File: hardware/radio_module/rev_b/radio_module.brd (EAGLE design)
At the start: 68.1 x 66 mm, 132 parts, among them J1 MODULE_GENERIC_DEBUGSMT, J2 TC2030-JLINK-NL, J3 U.FL-R-SMT, J4 NANO_SIM, J5 TC2030-JLINK-L, P1 MOLEX_73251-135X, P2 MOLEX_73251-135X, Q1 MOSFET-NCHANNELSMD, Q2 MOSFET-NCHANNELSMD, Q5 SI223DDS, Q6 SI223DDS, Q7 SI223DDS, Q8 MOSFET-NCHANNELSMD, U1 NUCLEUM, U10 XDOT_MODULE, U11 SAM4LC8BA, U12 UBLOX_SARA_G350, U2 TLV62130, U3 TXB0104RUT, U4 LTC2941, U5 LTC2941, U7 PCA9544AQFN-N20, U8 TLV62130, U9 LTC2941, X2 16 MHz

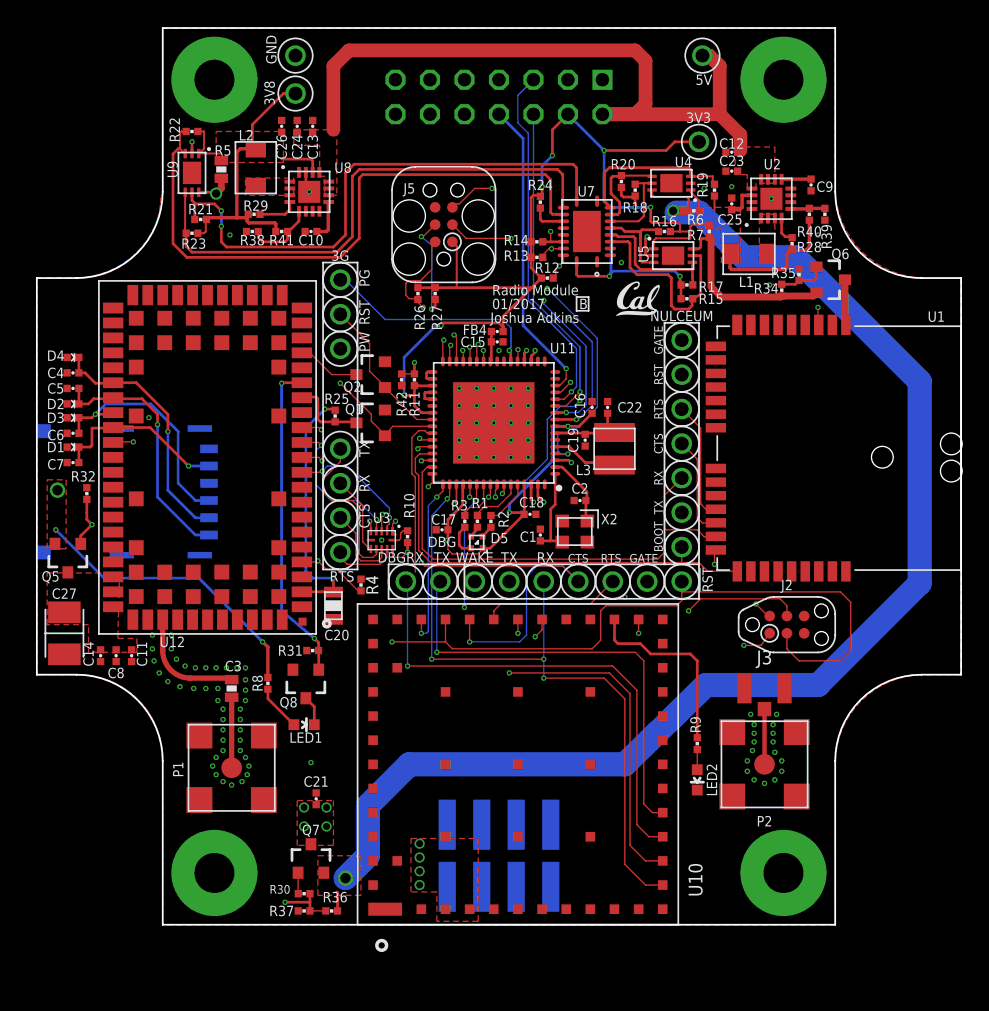
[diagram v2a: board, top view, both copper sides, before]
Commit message: added debugging signals, no more airwires
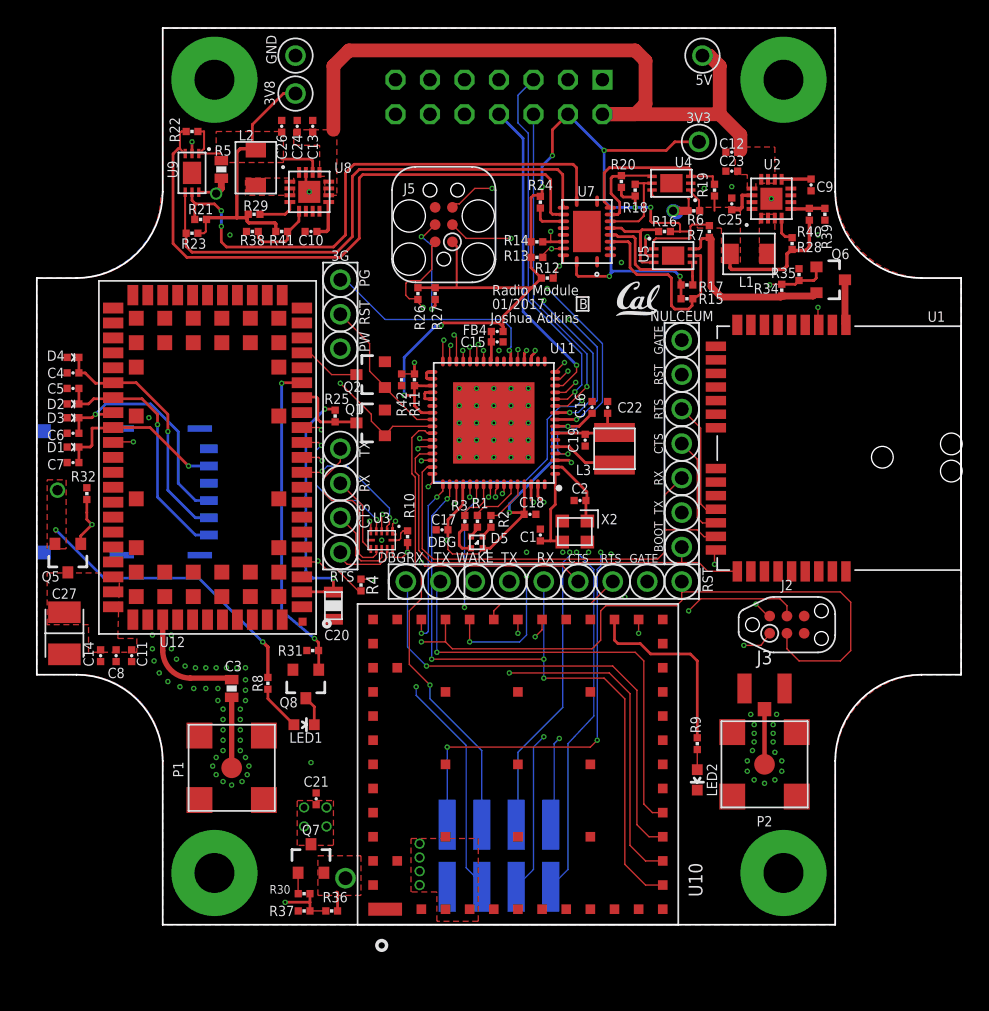
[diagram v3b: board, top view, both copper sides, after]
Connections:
- new net DBG_GPIO1: J1.16, U11.15
- new net DBG_GPIO2: J1.19, U11.16
- net !CONTROLLER_RESET: now also J1.20
- net CONTROLLER_SWDCLK: now also J1.21
- net CONTROLLER_SWDIO: now also J1.22
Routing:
- net DBG_GPIO1: track 0.00 -> 46.4 mm, vias 0 -> 4
- net DBG_GPIO2: track 0.00 -> 41.1 mm, vias 0 -> 3
- net CONTROLLER_SWDCLK: track 28.5 -> 65.1 mm, vias 4 -> 5
- net CONTROLLER_SWDIO: track 27.7 -> 61.0 mm, vias 3 -> 5
- net !CONTROLLER_RESET: track 26.6 -> 55.9 mm, vias 3 -> 4
- net DEBUG_TX: track 10.2 -> 37.3 mm, vias 1 -> 2
- net DEBUG_RX: track 11.8 -> 33.2 mm, vias 0 -> 1
- net XDOT_HOST_UART_RTS: track 23.7 -> 25.2 mm, vias 1 -> 3
- net XDOT_DBG_UART_TX: track 36.1 -> 35.3 mm
- net MOD_OUT: track 22.6 -> 23.3 mm
- net XDOT_HOST_UART_CTS: vias 3 -> 4
- net XDOT_3V3: vias 2 -> 3

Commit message: did a drc cleanup
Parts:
- moved U$1 4.06 mm to (44.1, 43.6)
- moved U3 1.09 mm to (28.6, 31.9)
- moved R10 1.05 mm to (30.4, 32.1)
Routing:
- net V_GSM_INT: track 13.5 -> 15.8 mm
- net NUCLEUM_POWER_GATE: track 43.0 -> 42.1 mm
- net N$22: track 9.52 -> 8.60 mm
- net N$23: track 9.93 -> 9.03 mm
- net XDOT_INT1: track 25.7 -> 26.6 mm
- net 3V3: track 167.3 -> 167.9 mm
- net GSM_RX: track 22.2 -> 21.6 mm
- net N$11: track 11.9 -> 11.3 mm
- net XDOT_HOST_UART_TX: track 51.0 -> 51.5 mm
- net XDOT_HOST_UART_RX: track 48.6 -> 49.1 mm
- net CONTROLLER_BUCK/LDO_N: track 21.7 -> 22.2 mm
- net XDOT_3V3: vias 3 -> 2
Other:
- board text added: "DBG RX"
- board text removed: "DBGRX"

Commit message: added sma antennas and fet gate resistors
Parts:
- removed R36: 100k, passives:0402_RES
- added J6: U.FL-R-SMT, connector:U.FL_SMT
- added R33: 100, passives:0402_RES
- added R43: 0, passives:0402_RES
- R34: value 100k -> 100
- moved LED1 9.51 mm to (13.7, 13.6), turned to 180 degrees
- moved R8 7.40 mm to (13.7, 16.1)
- moved C3 5.52 mm to (12.1, 22.1)
- moved R31 2.30 mm to (20.8, 22.5), turned to 90 degrees
- moved Q8 1.98 mm to (24.1, 21.6), turned to 0 degrees
- moved C21 1.81 mm to (24.8, 10.7)
- moved P1 1.61 mm to (18.7, 13.6), turned to 90 degrees
- moved C20 0.25 mm to (24.6, 26.3)
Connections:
- new net N$30: P1.1, R43.2
- new net N$31: Q5.1, R33.1
- new net N$32: Q6.1, R34.1
- net GND: now also J6.GND1, J6.GND2
- net GSM_POWER_GATE: now also R33.2; no longer Q5.1
- net N$7: now also J6.SIG, R43.1; no longer P1.1
- net NUCLEUM_3V3: no longer R34.2
- net NUCLEUM_POWER_GATE: now also R34.2; no longer Q6.1, R34.1
- net XDOT_3V3: no longer R36.2
- net XDOT_POWER_GATE: no longer R36.1
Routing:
- net N$13: track 2.21 -> 25.1 mm, vias 0 -> 2
- net N$30: track 0.00 -> 11.6 mm
- net N$6: track 8.24 -> 2.26 mm
- net GND: track 8.60 -> 13.5 mm, vias 101 -> 104
- net N$7: track 5.19 -> 8.12 mm
- net XDOT_POWER_GATE: track 77.1 -> 74.3 mm
- net NUCLEUM_3V3: track 13.8 -> 11.4 mm
- net N$8: track 3.41 -> 1.36 mm
- net NUCLEUM_POWER_GATE: track 42.1 -> 40.2 mm
- net XDOT_3V3: track 98.3 -> 96.9 mm
- net XDOT_GATED: track 38.0 -> 39.4 mm, vias 9 -> 8
- net GSM_LED: track 23.9 -> 25.2 mm
- net GSM_POWER_GATE: track 46.1 -> 45.5 mm
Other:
- board text added: "Populate for SMA"

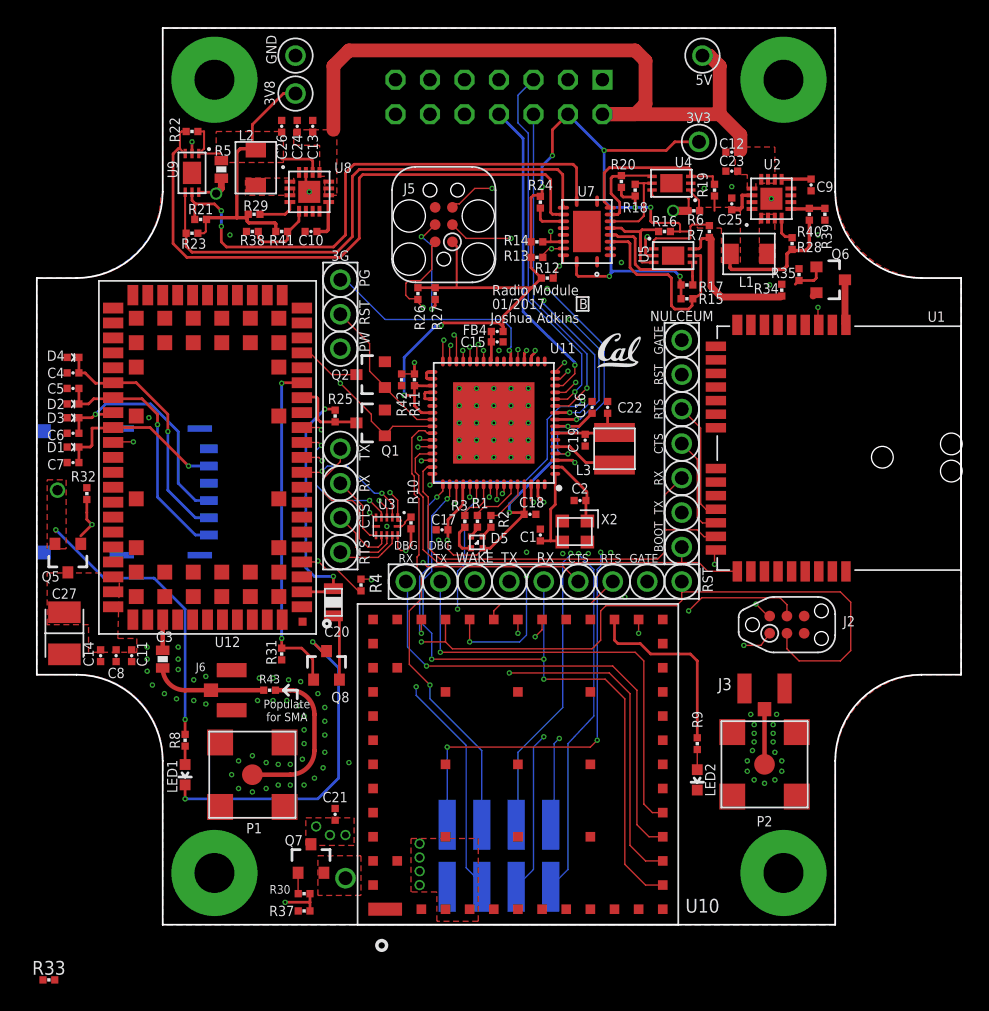
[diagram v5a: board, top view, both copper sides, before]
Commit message: added gate current limit resistors
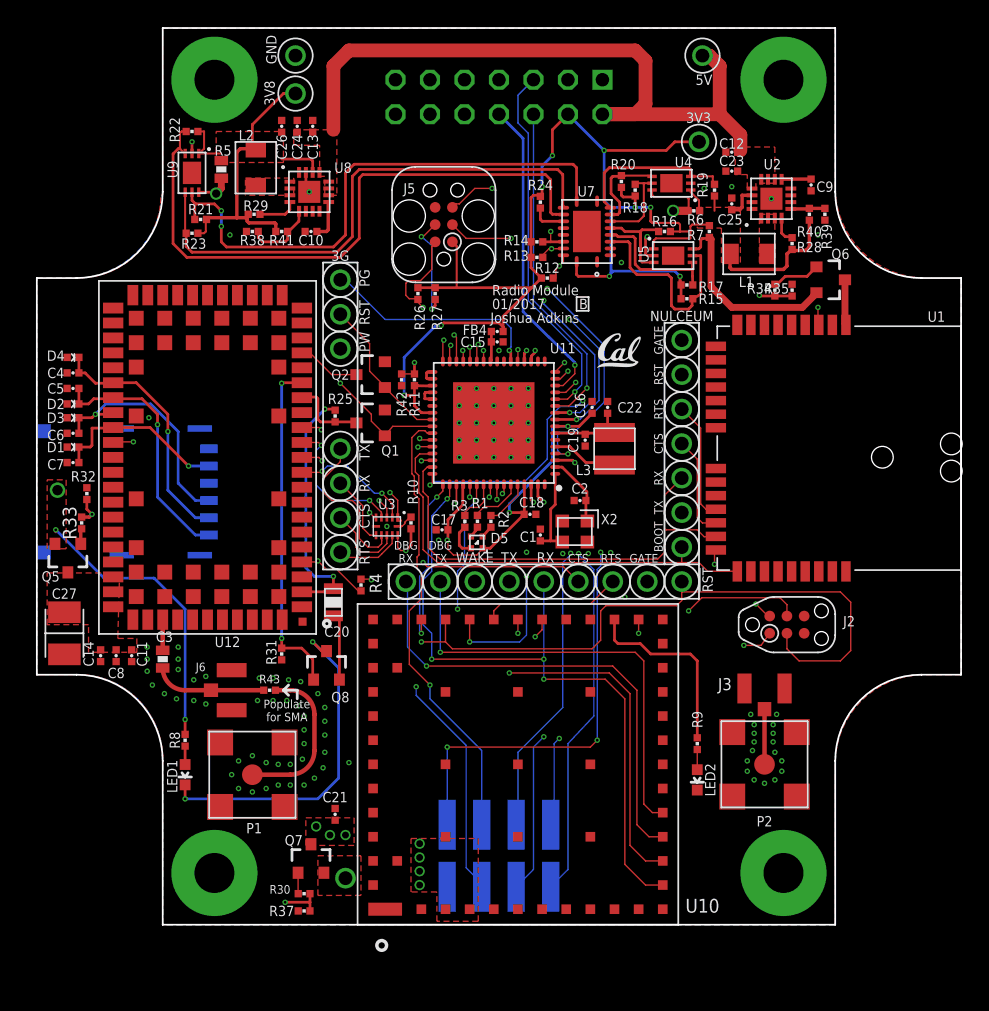
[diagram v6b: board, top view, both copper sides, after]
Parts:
- moved R33 33.7 mm to (6.10, 32.1), turned to 90 degrees
- moved R35 1.25 mm to (58.4, 49.3)
- moved R34 0.51 mm to (57.1, 49.3)
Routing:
- net N$32: track 0.00 -> 3.59 mm
- net NUCLEUM_3V3: track 11.4 -> 14.8 mm
- net GSM_POWER_GATE: track 45.5 -> 44.1 mm
- net NUCLEUM_POWER_GATE: track 40.2 -> 39.0 mm
- net N$31: track 0.00 -> 1.17 mm

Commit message: double checking rx/tx/rts/cts - fixed nucleum+labels
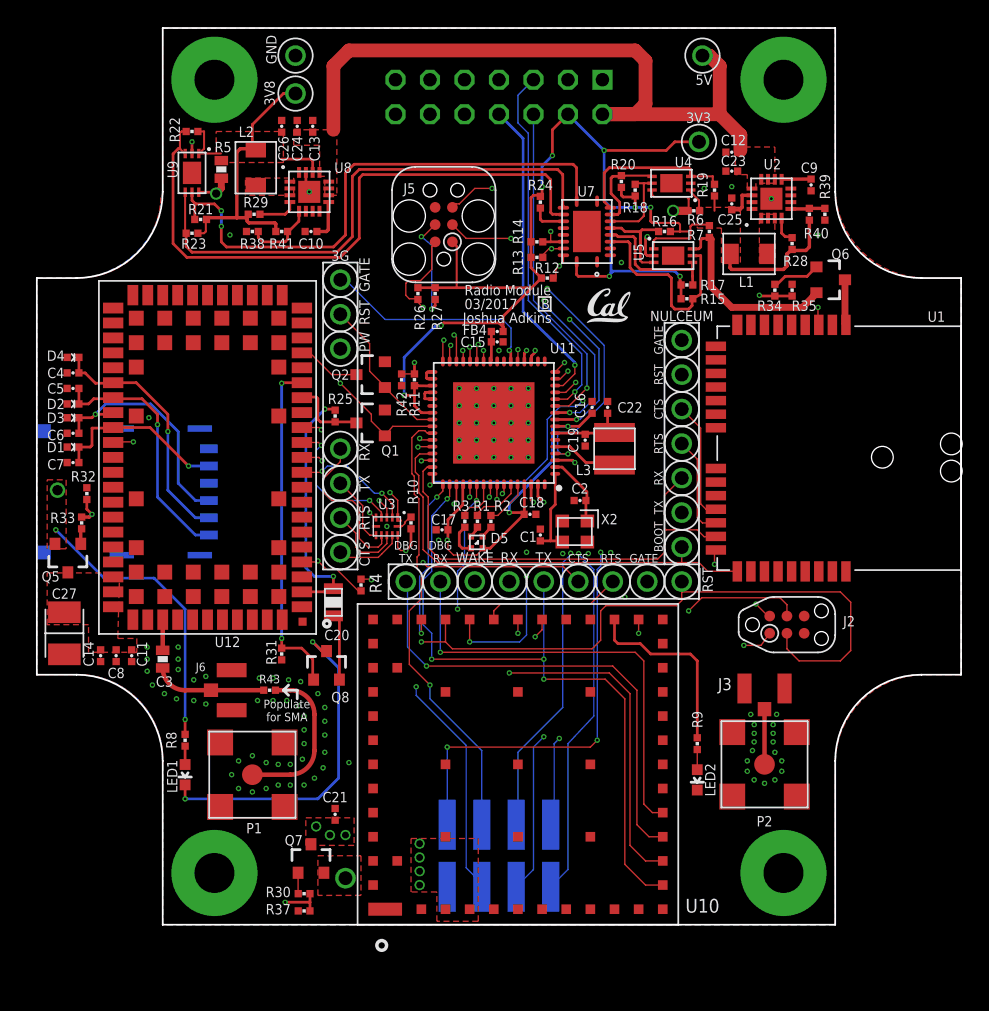
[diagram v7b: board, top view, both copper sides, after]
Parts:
- moved U$1 3.39 mm to (43.3, 46.9)
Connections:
- net NUCLEUM_INT1/RTS renamed NUCLEUM_INT1/CTS
- net NUCLEUM_INT2/CTS renamed NUCLEUM_INT2/RTS
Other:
- board text added: "03/2017"
- board text removed: "01/2017"
- board text removed: "PG"

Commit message: added attributes, renumbered, fixed up labels
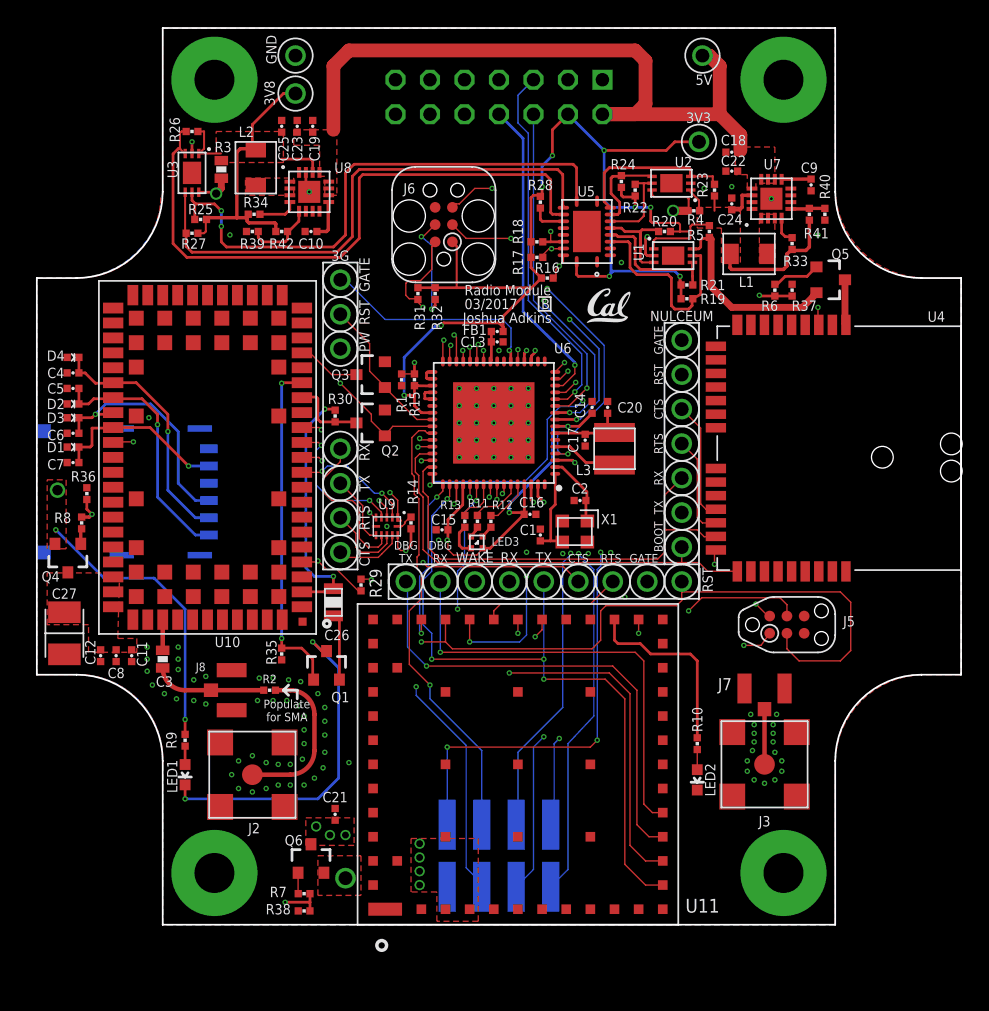
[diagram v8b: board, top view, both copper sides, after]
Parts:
- removed P1, P2: MOLEX_73251-135X, connector:SMA-J/PCB
- removed Q7: SI223DDS, fets:SOT23-3
- removed Q8: MOSFET-NCHANNELSMD, fets:SOT23-3
- removed R43: 0, passives:0402_RES
- removed TP28, TP29: TEST_POINT_0.040IN, headers:TESTPOINT_0.040IN
- removed U12: UBLOX_SARA_G350, signpost:UBLOX_SARA_G3
- added J7, J8: U.FL-R-SMT, connector:U.FL_SMT
- added Q3: MOSFET-NCHANNELSMD, fets:SOT23-3
- added Q4: SI223DDS, fets:SOT23-3
- added R36: 100k, passives:0402_RES
- added TP20, TP8: TEST_POINT_0.040IN, headers:TESTPOINT_0.040IN
- added U6: SAM4LC8BA, chips:QFN-64-9MM
- C12, C13: value 0.1uF -> 100nF
- C20: value 100uF -> 4.7uF; device passives:0805_CAP -> passives:0402_CAP
- C22: value 4.7uF -> 10uF
- C24: value 10uF -> 22uF
- C26: value 22uF -> 100uF; device passives:0402_CAP -> passives:0805_CAP
- D2, D3, D4: value (none) -> 14V
- J2: value TC2030-JLINK-NL -> MOLEX_73251-135X; device connector:TC2030-IDC-NL -> connector:SMA-J/PCB
- J3: value U.FL-R-SMT -> MOLEX_73251-135X; device connector:U.FL_SMT -> connector:SMA-J/PCB
- J5: value TC2030-JLINK-L -> TC2030-JLINK-NL; device connector:TC2030-IDC -> connector:TC2030-IDC-NL
- J6: value U.FL-R-SMT -> TC2030-JLINK-L; device connector:U.FL_SMT -> connector:TC2030-IDC
- R1, R2: value 1k -> 0
- R10, R11, R12, R13: value 10k -> 1k
- R25, R26, R27, R28, R29: value 100k -> 10k
- R3: value 1k -> 0.015; device passives:0402_RES -> passives:0603-RES
- R30, R33, R34: value 100 -> 100k
- R38: value 200k -> 100k
- R39: value 240k -> 200k
- R4: value 10k -> 0.43
- R40: value 750k -> 240k
- R42: value 0 -> 750k
- R5: value 0.015 -> 3.32; device passives:0603-RES -> passives:0402_RES
- R6: value 0.43 -> 100
- R7: value 3.32 -> 100
- R8: value 1k -> 100
- U1: value NUCLEUM -> LTC2941; device nucleum:NUCLEUM -> signpost:DFN-6-2MMX3MM
- U10: value XDOT_MODULE -> UBLOX_SARA_G350; device signpost:XDOT_MODULE -> signpost:UBLOX_SARA_G3
- U11: value SAM4LC8BA -> XDOT_MODULE; device chips:QFN-64-9MM -> signpost:XDOT_MODULE
- U2: value TLV62130 -> LTC2941; device chips:TQFN-16/3MM -> signpost:DFN-6-2MMX3MM
- U3: value TXB0104RUT -> LTC2941; device chips:UQFN-12 -> signpost:DFN-6-2MMX3MM
- U4: value LTC2941 -> NUCLEUM; device signpost:DFN-6-2MMX3MM -> nucleum:NUCLEUM
- U5: value LTC2941 -> PCA9544AQFN-N20; device signpost:DFN-6-2MMX3MM -> signpost:QFN-N20
- U7: value PCA9544AQFN-N20 -> TLV62130; device signpost:QFN-N20 -> chips:TQFN-16/3MM
- U9: value LTC2941 -> TXB0104RUT; device signpost:DFN-6-2MMX3MM -> chips:UQFN-12
- moved Q5 59.7 mm to (61.2, 50.0), turned to 270 degrees
- moved C12 59.5 mm to (7.49, 22.4), turned to 270 degrees
- moved R37 58.2 mm to (58.4, 49.3), turned to 270 degrees
- moved Q6 57.3 mm to (23.0, 7.37), turned to 0 degrees
- moved R7 57.2 mm to (22.5, 4.83), turned to 0 degrees
- moved R33 56.2 mm to (58.4, 52.7), turned to 270 degrees
- moved R38 50.2 mm to (22.5, 3.56)
- moved U10 48.9 mm to (15.4, 37.0)
- moved TP15 46.6 mm to (47.8, 27.8)
- moved R35 46.2 mm to (20.8, 22.5), turned to 90 degrees
- moved R39 42.2 mm to (18.7, 53.6), turned to 0 degrees
- moved J2 40.9 mm to (18.7, 13.6), turned to 90 degrees
- moved C14 40.6 mm to (43.7, 40.6), turned to 90 degrees
- moved TP2 40.3 mm to (21.8, 63.8)
- moved TP17 40.1 mm to (25.1, 30.0)
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- renumbered D5 to LED3, FB4 to FB1, X2 to X1
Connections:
- net !CONTROLLER_RESET: now also J6.3, U6.4; no longer J5.3, U11.4
- net !GSM_RST: now also Q3.1, TP21.TESTPOINT, U6.40; no longer Q2.1, TP24.TESTPOINT, U11.40
- net !NUCLEUM_RESET: now also TP5.TESTPOINT, U4.3, U6.13; no longer TP3.TESTPOINT, U1.3, U11.13
- net !XDOT_RESET: now also J5.3, TP24.TESTPOINT, U11.P$33, U6.30; no longer J2.3, TP7.TESTPOINT, U10.P$33, U11.30
- net 3V3: now also C14.1, C15.1, C24.2, J6.1, R14.2, R16.1, R17.1, R18.1, R21.2, R22.2, R23.2, R24.2, R28.1, R31.2, R32.2, R33.2, R4.2, R41.2, R5.2, TP1.TESTPOINT, U1.1, U2.1, U5.20, U6.35, U6.39, U6.52, U6.61, U6.8, U7.14, U9.11; no longer C17.1, C18.1, C25.2, J5.1, R10.2, R11.2, R12.1, R13.1, R14.1, R16.2, R17.2, R18.2, R24.1, R26.2, R27.2, R28.2, R40.2, R6.2, R7.2, TP17.TESTPOINT, U11.35, U11.39, U11.52, U11.61, U11.8, U2.14, U3.11, U4.1, U5.1, U7.20
- net 3V8: now also C25.2, R25.2, R26.2, R27.2, R3.2, R34.2, R42.2, TP2.TESTPOINT, U3.1; no longer C26.2, R21.2, R22.2, R23.2, R29.2, R41.2, R5.2, TP14.TESTPOINT, U9.1
- net 3VSWOUT: now also U7.1, U7.2, U7.3; no longer U2.1, U2.2, U2.3
- net 5V: now also C18.1, C19.1, C22.1, TP4.TESTPOINT, U7.10, U7.11, U7.12, U7.13; no longer C12.1, C13.1, C24.1, TP16.TESTPOINT, U2.10, U2.11, U2.12, U2.13
- net CONTROLLER_BUCK/LDO_N: now also R1.2, R15.1, U6.3; no longer R11.1, R42.2, U11.3
- net CONTROLLER_SWDCLK: now also J6.4, R32.1, U6.9; no longer J5.4, R27.1, U11.9
- net CONTROLLER_SWDIO: now also J6.2, R31.1, U6.10; no longer J5.2, R26.1, U11.10
- net CONTROLLER_XIN: now also U6.1; no longer U11.1
- net CONTROLLER_XOUT: now also U6.2; no longer U11.2
- net DBG_GPIO1: now also U6.15; no longer U11.15
- net DBG_GPIO2: now also U6.16; no longer U11.16
- net DEBUG_RX: now also U6.42; no longer U11.42
- net DEBUG_TX: now also U6.43; no longer U11.43
- net GND: now also C20.2, C24.1, C26.P$2, J2.2, J2.3, J2.4, J3.2, J3.3, J3.4, J3.5, J6.5, J7.GND1, J7.GND2, J8.GND1, J8.GND2, Q3.2, R1.1, R36.1, R40.1, TP3.TESTPOINT, U1.2, U10.P$14, U10.P$21, U10.P$22, U10.P$3, U10.P$30, U10.P$32, U10.P$33, U10.P$59, U10.P$60, U10.P$61, U10.P$63, U10.P$64, U10.P$9, U10.P65, U10.P66, U10.P67, U10.P68, U10.P69, U10.P70, U10.P71, U10.P72, U10.P73, U10.P74, U10.P75, U10.P76, U10.P77, U10.P78, U10.P79, U10.P80, U10.P81, U10.P82, U10.P83, U10.P84, U10.P85, U10.P86, U10.P87, U10.P88, U10.P89, U10.P90, U10.P91, U10.P92, U10.P93, U10.P94, U10.P95, U10.P96, U11.P$1, U11.P$17, U11.P$20, U11.P$35, U11.P$36, U11.P$38, U11.P$39, U11.P$40, U11.P$41, U11.P$42, U11.P$43, U11.P$44, U11.P$45, U11.P$46, U11.P$48, U11.P$49, U11.P$5, U11.P$50, U11.P$51, U11.P$52, U11.P$53, U11.P$54, U11.P$55, U11.P$56, U11.P$57, U11.P$58, U2.2, U3.2, U4.32, U5.1, U5.10, U5.3, U6.23, U6.38, U6.6, U6.64, U6.GND, U7.15, U7.16, U7.6, U7.7, U7.8, U7.GND, U9.6; no longer C20.P$2, C24.2, C26.1, J3.GND1, J3.GND2, J6.GND1, J6.GND2, P1.2, P1.3, P1.4, P1.5, P2.2, P2.3, P2.4, P2.5, Q8.2, R31.1, R32.1, R42.1, TP15.TESTPOINT, U1.32, U10.P$17, U10.P$35, U10.P$36, U10.P$38, U10.P$39, U10.P$40, U10.P$41, U10.P$42, U10.P$44, U10.P$45, U10.P$46, U10.P$48, U10.P$49, U10.P$51, U10.P$52, U10.P$53, U10.P$56, U11.23, U11.38, U11.6, U11.64, U11.GND, U12.P$1, U12.P$14, U12.P$20, U12.P$21, U12.P$22, U12.P$3, U12.P$30, U12.P$32, U12.P$33, U12.P$43, U12.P$5, U12.P$50, U12.P$54, U12.P$55, U12.P$57, U12.P$58, U12.P$59, U12.P$60, U12.P$61, U12.P$63, U12.P$64, U12.P$9, U12.P65, U12.P66, U12.P67, U12.P68, U12.P69, U12.P70, U12.P71, U12.P72, U12.P73, U12.P74, U12.P75, U12.P76, U12.P77, U12.P78, U12.P79, U12.P80, U12.P81, U12.P82, U12.P83, U12.P84, U12.P85, U12.P86, U12.P87, U12.P88, U12.P89, U12.P90, U12.P91, U12.P92, U12.P93, U12.P94, U12.P95, U12.P96, U2.15, U2.16, U2.6, U2.7, U2.8, U2.GND, U3.6, U4.2, U7.1, U7.10, U7.2, U7.3, U9.2
- net GSM_3V8: now also Q4.2, R3.1, R9.2, U3.6; no longer Q5.2, R5.1, R8.2, U9.6
- net GSM_CTS: now also TP18.TESTPOINT, U6.29, U9.9; no longer TP21.TESTPOINT, U11.29, U3.9
- net GSM_GATED: now also C12.1, Q4.3, U10.P$51, U10.P$52, U10.P$53; no longer C14.1, Q5.3, U12.P$51, U12.P$52, U12.P$53
- net GSM_GAUGE_ALERT: now also R25.1, U3.5, U5.11; no longer R21.1, U7.11, U9.5
- net GSM_GAUGE_SCL: now also R26.1, U3.3, U5.13; no longer R22.1, U7.13, U9.3
- net GSM_GAUGE_SDA: now also R27.1, U3.4, U5.12; no longer R23.1, U7.12, U9.4
- net GSM_LED: now also Q1.1, R35.2, U10.P$16; no longer Q8.1, R31.2, U12.P$16
- net GSM_POWER: now also Q2.1, TP22.TESTPOINT, U6.41; no longer Q1.1, TP25.TESTPOINT, U11.41
- net GSM_POWER_GATE: now also R36.2, R8.2, TP16.TESTPOINT, U6.22; no longer R32.2, R33.2, TP5.TESTPOINT, U11.22
- net GSM_RTS: now also TP17.TESTPOINT, U6.26, U9.10; no longer TP13.TESTPOINT, U11.26, U3.10
- net GSM_RX: now also TP19.TESTPOINT, U6.31, U9.7; no longer TP22.TESTPOINT, U11.31, U3.7
- net GSM_TX: now also TP20.TESTPOINT, U6.32, U9.8; no longer TP23.TESTPOINT, U11.32, U3.8
- net IM880_GAUGE_ALERT: now also R22.1, U2.5, U5.7; no longer R18.1, U4.5, U7.7
- net IM880_GAUGE_SCL: now also R23.1, U2.3, U5.9; no longer R19.1, U4.3, U7.9
- net IM880_GAUGE_SDA: now also R24.1, U2.4, U5.8; no longer R20.1, U4.4, U7.8
- net MOD_IN: now also U6.20; no longer U11.20
- net MOD_OUT: now also U6.14; no longer U11.14
- net N$1: now also U10.P$41; no longer U12.P$41
- net N$10: now also U10.P$12, U9.4; no longer U12.P$12, U3.4
- net N$11: now also U10.P$13, U9.5; no longer U12.P$13, U3.5
- net N$12: now also R28.2, U5.14; no longer R24.2, U7.14
- net N$13: now also Q1.3; no longer Q8.3
- net N$14: now also Q3.3, U10.P$18; no longer Q2.3, U12.P$18
- net N$15: now also C26.P$1, R30.2, U10.P$2; no longer C20.P$1, R25.2, U12.P$2
- net N$16: now also Q2.3, R30.1, U10.P$15; no longer Q1.3, R25.1, U12.P$15
- net N$17: now also R11.1, U6.59; no longer R1.1, U11.59
- net N$18: now also R11.2; no longer R1.2
- net N$19: now also Q5.3, U4.1; no longer Q6.3, U1.1
- net N$2: now also U10.P$40; no longer U12.P$40
- net N$20: now also R12.2; no longer R2.2
- net N$21: now also R13.2; no longer R3.2
- net N$22: now also U10.P$11, U9.3; no longer U12.P$11, U3.3
- net N$23: now also U10.P$10, U9.2; no longer U12.P$10, U3.2
- net N$24: now also J3.1, J7.SIG; no longer J3.SIG, P2.1
- net N$25: now also R12.1, U6.60; no longer R2.1, U11.60
- net N$26: now also R13.1, U6.55; no longer R3.1, U11.55
- net N$27: now also R10.1; no longer R9.1
- net N$28: now also Q6.1, R7.1; no longer Q7.1, R30.1
- net N$29: now also R29.1, U10.P$42; no longer R4.1, U12.P$42
- net N$3: now also U10.P$39; no longer U12.P$39
- net N$30: now also J2.1, R2.2; no longer P1.1, R43.2
- net N$31: now also Q4.1, R8.1; no longer Q5.1, R33.1
- net N$32: now also Q5.1, R6.1; no longer Q6.1, R34.1
- net N$33: now also C13.1, U6.25; no longer C15.1, U11.25
- net N$34: now also U7.9; no longer U2.9
- net N$36: now also R33.1, U7.4; no longer R28.1, U2.4
- net N$37: now also R40.2, R41.1, U7.5; no longer R39.2, R40.1, U2.5
- net N$4: now also U10.P$38; no longer U12.P$38
- net N$40: now also R34.1; no longer R29.1
- net N$41: now also R39.2, R42.1; no longer R38.2, R41.1
- net N$44: now also C17.1, C20.1, U6.7; no longer C19.1, C22.1, U11.7
- net N$5: now also R14.1, U9.12; no longer R10.1, U3.12
- net N$52: now also U6.5; no longer U11.5
- net N$53: now also U6.36, U6.37; no longer U11.36, U11.37
- net N$54: now also U6.33, U6.34; no longer U11.33, U11.34
- net N$6: now also U10.P$56; no longer U12.P$56
- net N$7: now also J8.SIG, R2.1; no longer J6.SIG, R43.1
- net N$8: now also R9.1; no longer R8.1
- net N$9: now also R18.2, U5.17, U6.53; no longer R14.2, U11.53, U7.17
- net NUCLEUM_3V3: now also Q5.2, R5.1, U1.6; no longer Q6.2, R7.1, U5.6
- net NUCLEUM_BOOT: now also TP8.TESTPOINT, U4.24, U6.45; no longer TP11.TESTPOINT, U1.24, U11.45
- net NUCLEUM_GAUGE_ALERT: now also R19.1, U1.5, U5.4; no longer R15.1, U5.5, U7.4
- net NUCLEUM_GAUGE_SCL: now also R20.1, U1.3, U5.6; no longer R16.1, U5.3, U7.6
- net NUCLEUM_GAUGE_SDA: now also R21.1, U1.4, U5.5; no longer R17.1, U5.4, U7.5
- net NUCLEUM_INT1/CTS: now also TP6.TESTPOINT, U4.20, U6.27; no longer TP9.TESTPOINT, U1.20, U11.27
- net NUCLEUM_INT2/RTS: now also TP7.TESTPOINT, U4.21, U6.28; no longer TP10.TESTPOINT, U1.21, U11.28
- net NUCLEUM_POWER_GATE: now also R37.2, R6.2, TP11.TESTPOINT, U6.48; no longer R34.2, R35.2, TP19.TESTPOINT, U11.48
- net NUCLEUM_RX: now also TP10.TESTPOINT, U4.22, U6.47; no longer TP18.TESTPOINT, U1.22, U11.47
- net NUCLEUM_TX: now also TP9.TESTPOINT, U4.23, U6.46; no longer TP12.TESTPOINT, U1.23, U11.46
- net PPS: now also U6.19; no longer U11.19
- net SCL: now also U6.12; no longer U11.12
- net SCL_INTERNAL: now also R17.2, U5.18, U6.58; no longer R13.2, U11.58, U7.18
- net SDA: now also U6.11; no longer U11.11
- net SDA_INTERNAL: now also R16.2, U5.19, U6.57; no longer R12.2, U11.57, U7.19
- net USB_D+: now also U6.63; no longer U11.63
- net USB_D-: now also U6.62; no longer U11.62
- net V_GSM_INT: now also R29.2, U10.P$4, U9.1; no longer R4.2, U12.P$4, U3.1
- net XDOT_3V3: now also Q6.2, R4.1, U2.6; no longer Q7.2, R6.1, U4.6
- net XDOT_DBG_UART_RX: now also TP27.TESTPOINT, U11.P$16; no longer TP29.TESTPOINT, U10.P$16
- net XDOT_DBG_UART_TX: now also TP26.TESTPOINT, U11.P$15; no longer TP28.TESTPOINT, U10.P$15
- net XDOT_GATED: now also J5.1, Q6.3, U11.P$3, U11.P$4; no longer J2.1, Q7.3, U10.P$3, U10.P$4
- net XDOT_GPIO0: now also R10.2, U11.P$26; no longer R9.2, U10.P$26
- net XDOT_HOST_UART_CTS: now also TP25.TESTPOINT, U11.P$32, U6.44; no longer TP27.TESTPOINT, U10.P$32, U11.44
- net XDOT_HOST_UART_RTS: now also TP23.TESTPOINT, U11.P$31, U6.56; no longer TP26.TESTPOINT, U10.P$31, U11.56
- net XDOT_HOST_UART_RX: now also TP12.TESTPOINT, U11.P$14, U6.51; no longer TP1.TESTPOINT, U10.P$14, U11.51
- net XDOT_HOST_UART_TX: now also TP13.TESTPOINT, U11.P$13, U6.50; no longer TP2.TESTPOINT, U10.P$13, U11.50
- net XDOT_INT1: now also U11.P$25, U6.54; no longer U10.P$25, U11.54
- net XDOT_POWER_GATE: now also R38.2, R7.2, TP15.TESTPOINT, U6.21; no longer R30.2, R37.2, TP4.TESTPOINT, U11.21
- net XDOT_SWCLK: now also J5.4, U11.P$29; no longer J2.4, U10.P$29
- net XDOT_SWDIO: now also J5.2, U11.P$30; no longer J2.2, U10.P$30
- net XDOT_WAKE: now also TP14.TESTPOINT, U11.P$34, U6.49; no longer TP6.TESTPOINT, U10.P$34, U11.49
